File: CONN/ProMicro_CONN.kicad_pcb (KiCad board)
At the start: 2 copper layers, 17.8 x 30.5 mm, 20 parts, among them J1 AVR-JTAG-10, J2 UEXT_Host, J3 Display, SW1 reset, SW2 user

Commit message: dump
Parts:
- removed C1: 1µ, Capacitor_SMD:C_0603_1608Metric
- A1: value Sparkfun_Pro_Micro_3V3 -> Sparkfun_Pro_Micro
- LOGO1: footprint Symbol:OSHW-Logo2_7.3x6mm_SilkScreen -> Symbol:OSHW-Symbol_6.7x6mm_SilkScreen
- moved LOGO1 0.25 mm to (144.8, 81.3)
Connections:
- net A0 renamed TDI
- net A1 renamed TDO
- net A2 renamed TMS
- net A3 renamed TCK
- net D0 renamed TXD
- net D1 renamed RXD
- net D14 renamed CIPO
- net D15 renamed SCK
- net D16 renamed COPI
- net D2 renamed SDA
- net D3 renamed SCL
- net D9 renamed CS1
- net Reset renamed ~RST
- A1 pad 3: (no net) -> GND
- A1 pad 8: D5 -> (no net)
- A1 pad 9: (no net) -> BTN
- R9 pad 1: D5 -> BTN
- SW2 pad 2: D5 -> BTN
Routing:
- net BTN: track 0.00 -> 23.9 mm, vias 0 -> 1
- net D5: track 21.8 -> 0.00 mm, vias 1 -> 0
- net SDA: track 52.4 -> 52.9 mm
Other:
- board text removed: "3V3"
- board text removed: "A0"
- board text removed: "A1"
- board text removed: "A2"
- board text removed: "A3"
- board text removed: "CS0i"
- board text removed: "CS1e"
- board text removed: "D0"
- board text removed: "D1"
- board text removed: "D10"
- board text removed: "D14"
- board text removed: "D15"
- board text removed: "D16"
- board text removed: "D2"
- board text removed: "D3"
- board text removed: "D4"
- board text removed: "D5"
- board text removed: "D6"
- board text removed: "D7"
- board text removed: "D8"
- board text removed: "D9"
- board text removed: "GND"
- board text removed: "MISO"
- board text removed: "MOSI"
- board text removed: "RXD"
- board text removed: "SCK"
- board text removed: "SCL"
- board text removed: "SDA"
- board text removed: "TCK"
- board text removed: "TDI"
- board text removed: "TDO"
- board text removed: "TMS"
- board text removed: "TXD"
- board text removed: "VCC"
- board text removed: "~Reset"

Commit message: clean
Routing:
- net TCK: track 23.5 -> 22.9 mm
- net GND: vias 25 -> 20

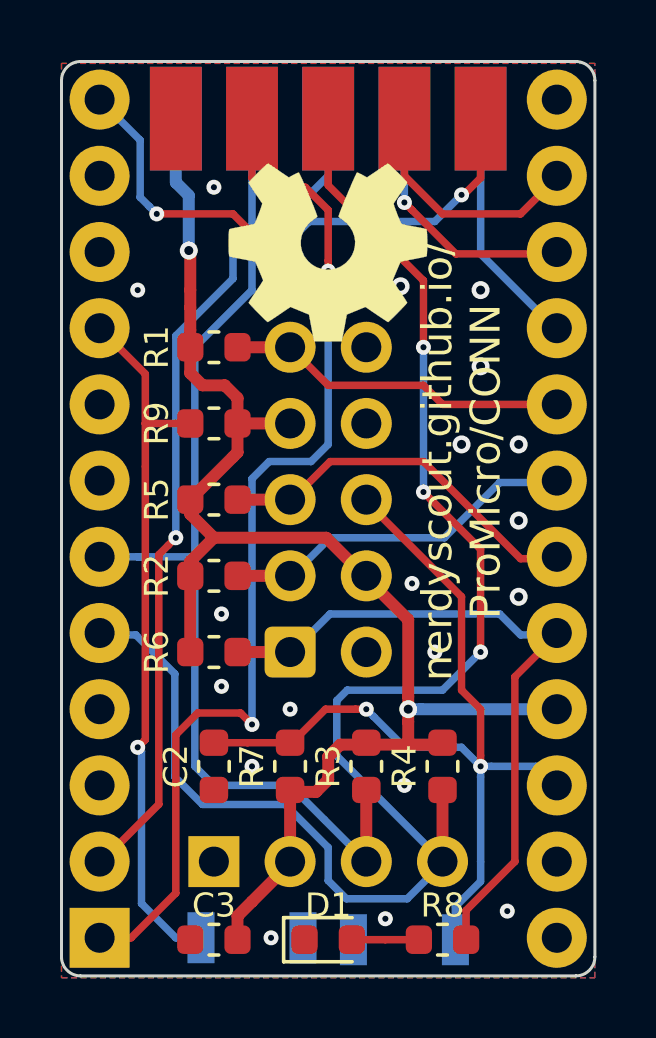
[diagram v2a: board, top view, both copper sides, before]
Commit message: make controller holes wide enough
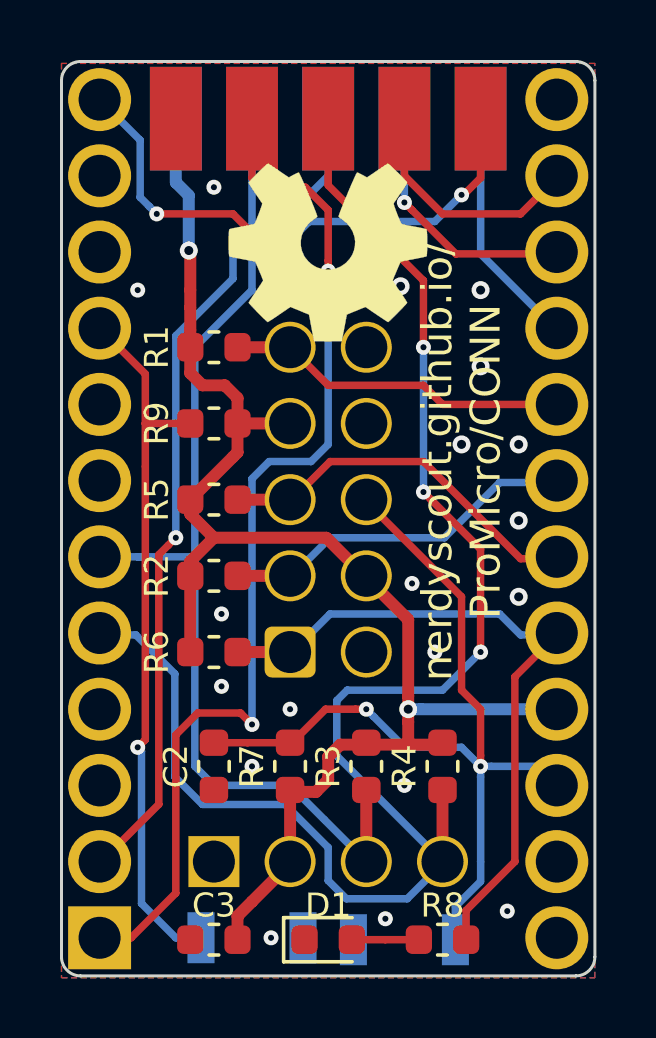
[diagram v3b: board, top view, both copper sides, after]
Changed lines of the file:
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@@
-(kicad_pcb (version 20171130) (host pcbnew 5.1.5+dfsg1-2build2)
+(kicad_pcb (version 20171130) (host pcbnew 5.1.5)
   (general
     (thickness 0.8)
@@
       (effects (font (size 1 1) (thickness 0.15)) (justify mirror))
     )
-    (pad 1 thru_hole rect (at 0 0) (size 2 2) (drill 1) (layers *.Cu *.Mask)
+    (pad 1 thru_hole rect (at 0 0) (size 2.1 2.1) (drill 1.4) (layers *.Cu *.Mask)
       (net 4 RXD))
-    (pad 2 thru_hole oval (at 0 -2.54) (size 2 2) (drill 1) (layers *.Cu *.Mask)
+    (pad 2 thru_hole circle (at 0 -2.54) (size 2.1 2.1) (drill 1.4) (layers *.Cu *.Mask)
       (net 5 TXD))
-    (pad 3 thru_hole oval (at 0 -5.08) (size 2 2) (drill 1) (layers *.Cu *.Mask)
-      (net 1 GND))
-    (pad 13 thru_hole oval (at 15.24 -27.94) (size 2 2) (drill 1) (layers *.Cu *.Mask))
-    (pad 4 thru_hole oval (at 0 -7.62) (size 2 2) (drill 1) (layers *.Cu *.Mask)
-      (net 1 GND))
-    (pad 14 thru_hole oval (at 15.24 -25.4) (size 2 2) (drill 1) (layers *.Cu *.Mask)
+    (pad 3 thru_hole circle (at 0 -5.08) (size 2.1 2.1) (drill 1.4) (layers *.Cu *.Mask)
+      (net 1 GND))
+    (pad 13 thru_hole circle (at 15.24 -27.94) (size 2.1 2.1) (drill 1.4) (layers *.Cu *.Mask))
+    (pad 4 thru_hole circle (at 0 -7.62) (size 2.1 2.1) (drill 1.4) (layers *.Cu *.Mask)
+      (net 1 GND))
+    (pad 14 thru_hole circle (at 15.24 -25.4) (size 2.1 2.1) (drill 1.4) (layers *.Cu *.Mask)
       (net 6 COPI))
-    (pad 5 thru_hole oval (at 0 -10.16) (size 2 2) (drill 1) (layers *.Cu *.Mask)
+    (pad 5 thru_hole circle (at 0 -10.16) (size 2.1 2.1) (drill 1.4) (layers *.Cu *.Mask)
       (net 7 SDA))
-    (pad 15 thru_hole oval (at 15.24 -22.86) (size 2 2) (drill 1) (layers *.Cu *.Mask)
+    (pad 15 thru_hole circle (at 15.24 -22.86) (size 2.1 2.1) (drill 1.4) (layers *.Cu *.Mask)
       (net 8 CIPO))
-    (pad 6 thru_hole oval (at 0 -12.7) (size 2 2) (drill 1) (layers *.Cu *.Mask)
+    (pad 6 thru_hole circle (at 0 -12.7) (size 2.1 2.1) (drill 1.4) (layers *.Cu *.Mask)
       (net 9 SCL))
-    (pad 16 thru_hole oval (at 15.24 -20.32) (size 2 2) (drill 1) (layers *.Cu *.Mask)
+    (pad 16 thru_hole circle (at 15.24 -20.32) (size 2.1 2.1) (drill 1.4) (layers *.Cu *.Mask)
       (net 10 SCK))
-    (pad 7 thru_hole oval (at 0 -15.24) (size 2 2) (drill 1) (layers *.Cu *.Mask))
-    (pad 17 thru_hole oval (at 15.24 -17.78) (size 2 2) (drill 1) (layers *.Cu *.Mask)
+    (pad 7 thru_hole circle (at 0 -15.24) (size 2.1 2.1) (drill 1.4) (layers *.Cu *.Mask))
+    (pad 17 thru_hole circle (at 15.24 -17.78) (size 2.1 2.1) (drill 1.4) (layers *.Cu *.Mask)
       (net 11 TDI))
-    (pad 8 thru_hole oval (at 0 -17.78) (size 2 2) (drill 1) (layers *.Cu *.Mask))
-    (pad 18 thru_hole oval (at 15.24 -15.24) (size 2 2) (drill 1) (layers *.Cu *.Mask)
+    (pad 8 thru_hole circle (at 0 -17.78) (size 2.1 2.1) (drill 1.4) (layers *.Cu *.Mask))
+    (pad 18 thru_hole circle (at 15.24 -15.24) (size 2.1 2.1) (drill 1.4) (layers *.Cu *.Mask)
       (net 12 TDO))
-    (pad 9 thru_hole oval (at 0 -20.32) (size 2 2) (drill 1) (layers *.Cu *.Mask)
+    (pad 9 thru_hole circle (at 0 -20.32) (size 2.1 2.1) (drill 1.4) (layers *.Cu *.Mask)
       (net 13 BTN))
-    (pad 19 thru_hole oval (at 15.24 -12.7) (size 2 2) (drill 1) (layers *.Cu *.Mask)
+    (pad 19 thru_hole circle (at 15.24 -12.7) (size 2.1 2.1) (drill 1.4) (layers *.Cu *.Mask)
       (net 14 TMS))
-    (pad 10 thru_hole oval (at 0 -22.86) (size 2 2) (drill 1) (layers *.Cu *.Mask))
-    (pad 20 thru_hole oval (at 15.24 -10.16) (size 2 2) (drill 1) (layers *.Cu *.Mask)
+    (pad 10 thru_hole circle (at 0 -22.86) (size 2.1 2.1) (drill 1.4) (layers *.Cu *.Mask))
+    (pad 20 thru_hole circle (at 15.24 -10.16) (size 2.1 2.1) (drill 1.4) (layers *.Cu *.Mask)
       (net 15 TCK))
-    (pad 11 thru_hole oval (at 0 -25.4) (size 2 2) (drill 1) (layers *.Cu *.Mask))
-    (pad 21 thru_hole oval (at 15.24 -7.62) (size 2 2) (drill 1) (layers *.Cu *.Mask)
-      (net 2 +3V3))
-    (pad 12 thru_hole oval (at 0 -27.94) (size 2 2) (drill 1) (layers *.Cu *.Mask)
+    (pad 11 thru_hole circle (at 0 -25.4) (size 2.1 2.1) (drill 1.4) (layers *.Cu *.Mask))
+    (pad 21 thru_hole circle (at 15.24 -7.62) (size 2.1 2.1) (drill 1.4) (layers *.Cu *.Mask)
+      (net 2 +3V3))
+    (pad 12 thru_hole circle (at 0 -27.94) (size 2.1 2.1) (drill 1.4) (layers *.Cu *.Mask)
       (net 16 CS1))
-    (pad 22 thru_hole oval (at 15.24 -5.08) (size 2 2) (drill 1) (layers *.Cu *.Mask)
+    (pad 22 thru_hole circle (at 15.24 -5.08) (size 2.1 2.1) (drill 1.4) (layers *.Cu *.Mask)
       (net 17 ~RST))
-    (pad 23 thru_hole oval (at 15.24 -2.54) (size 2 2) (drill 1) (layers *.Cu *.Mask)
-      (net 1 GND))
-    (pad 24 thru_hole oval (at 15.24 0) (size 2 2) (drill 1) (layers *.Cu *.Mask))
+    (pad 23 thru_hole circle (at 15.24 -2.54) (size 2.1 2.1) (drill 1.4) (layers *.Cu *.Mask)
+      (net 1 GND))
+    (pad 24 thru_hole circle (at 15.24 0) (size 2.1 2.1) (drill 1.4) (layers *.Cu *.Mask))
     (model ${KISYS3DMOD}/Module.3dshapes/Sparkfun_Pro_Micro.wrl
       (at (xyz 0 0 0))
@@
     (fp_line (start -2.18 5.1) (end 5.72 5.1) (layer B.Fab) (width 0.1))
     (fp_line (start -3.18 4.1) (end -2.18 5.1) (layer B.Fab) (width 0.1))
-    (pad 10 thru_hole circle (at 2.54 -10.16) (size 1.7 1.7) (drill 1) (layers *.Cu *.Mask)
-      (net 1 GND))
-    (pad 8 thru_hole circle (at 2.54 -7.62) (size 1.7 1.7) (drill 1) (layers *.Cu *.Mask))
-    (pad 6 thru_hole circle (at 2.54 -5.08) (size 1.7 1.7) (drill 1) (layers *.Cu *.Mask)
+    (pad 10 thru_hole circle (at 2.54 -10.16) (size 1.7 1.7) (drill 1.4) (layers *.Cu *.Mask)
+      (net 1 GND))
+    (pad 8 thru_hole circle (at 2.54 -7.62) (size 1.7 1.7) (drill 1.4) (layers *.Cu *.Mask))
+    (pad 6 thru_hole circle (at 2.54 -5.08) (size 1.7 1.7) (drill 1.4) (layers *.Cu *.Mask)
       (net 17 ~RST))
-    (pad 4 thru_hole circle (at 2.54 -2.54) (size 1.7 1.7) (drill 1) (layers *.Cu *.Mask)
-      (net 2 +3V3))
-    (pad 2 thru_hole circle (at 2.54 0) (size 1.7 1.7) (drill 1) (layers *.Cu *.Mask)
-      (net 1 GND))
-    (pad 9 thru_hole circle (at 0 -10.16) (size 1.7 1.7) (drill 1) (layers *.Cu *.Mask)
+    (pad 4 thru_hole circle (at 2.54 -2.54) (size 1.7 1.7) (drill 1.4) (layers *.Cu *.Mask)
+      (net 2 +3V3))
+    (pad 2 thru_hole circle (at 2.54 0) (size 1.7 1.7) (drill 1.4) (layers *.Cu *.Mask)
+      (net 1 GND))
+    (pad 9 thru_hole circle (at 0 -10.16) (size 1.7 1.7) (drill 1.4) (layers *.Cu *.Mask)
       (net 11 TDI))
-    (pad 7 thru_hole circle (at 0 -7.62) (size 1.7 1.7) (drill 1) (layers *.Cu *.Mask)
-      (net 2 +3V3))
-    (pad 5 thru_hole circle (at 0 -5.08) (size 1.7 1.7) (drill 1) (layers *.Cu *.Mask)
+    (pad 7 thru_hole circle (at 0 -7.62) (size 1.7 1.7) (drill 1.4) (layers *.Cu *.Mask)
+      (net 2 +3V3))
+    (pad 5 thru_hole circle (at 0 -5.08) (size 1.7 1.7) (drill 1.4) (layers *.Cu *.Mask)
       (net 14 TMS))
-    (pad 3 thru_hole circle (at 0 -2.54) (size 1.7 1.7) (drill 1) (layers *.Cu *.Mask)
+    (pad 3 thru_hole circle (at 0 -2.54) (size 1.7 1.7) (drill 1.4) (layers *.Cu *.Mask)
       (net 12 TDO))
-    (pad 1 thru_hole roundrect (at 0 0) (size 1.7 1.7) (drill 1) (layers *.Cu *.Mask) (roundrect_rratio 0.147059)
+    (pad 1 thru_hole roundrect (at 0 0) (size 1.7 1.7) (drill 1.4) (layers *.Cu *.Mask) (roundrect_rratio 0.147059)
       (net 15 TCK))
     (model ${KISYS3DMOD}/Connector_IDC.3dshapes/IDC-Header_2x05_P2.54mm_Vertical.wrl
@@
       (effects (font (size 0.8 0.8) (thickness 0.2)) (justify mirror))
     )
-    (pad 4 thru_hole oval (at 0 -7.62 270) (size 1.7 1.7) (drill 1) (layers *.Cu *.Mask)
+    (pad 4 thru_hole circle (at 0 -7.62 270) (size 1.7 1.7) (drill 1.4) (layers *.Cu *.Mask)
       (net 7 SDA))
-    (pad 3 thru_hole oval (at 0 -5.08 270) (size 1.7 1.7) (drill 1) (layers *.Cu *.Mask)
+    (pad 3 thru_hole circle (at 0 -5.08 270) (size 1.7 1.7) (drill 1.4) (layers *.Cu *.Mask)
       (net 9 SCL))
-    (pad 2 thru_hole oval (at 0 -2.54 270) (size 1.7 1.7) (drill 1) (layers *.Cu *.Mask)
-      (net 2 +3V3))
-    (pad 1 thru_hole rect (at 0 0 270) (size 1.7 1.7) (drill 1) (layers *.Cu *.Mask)
+    (pad 2 thru_hole circle (at 0 -2.54 270) (size 1.7 1.7) (drill 1.4) (layers *.Cu *.Mask)
+      (net 2 +3V3))
+    (pad 1 thru_hole rect (at 0 0 270) (size 1.7 1.7) (drill 1.4) (layers *.Cu *.Mask)
       (net 1 GND))
     (model ${KISYS3DMOD}/Connector_PinHeader_2.54mm.3dshapes/PinHeader_1x04_P2.54mm_Vertical.wrl
